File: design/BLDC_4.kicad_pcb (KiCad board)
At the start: 2 copper layers, 233 parts, among them K1 SERVO, P1 CANBUS, P10 MOTOR3, P11 MOTOR2, P12 MOTOR1, P13 SWD, P14 IN+, P15 PWR_COMM, P2 HALL/Encoder, P3 HALL/Encoder, P4 PWR_COMM, P5 IN+, P6 IN-, P7 MOTOR3, P8 MOTOR2, P9 MOTOR1, Q1 IRFS3006, Q10 IRFS3006, Q11 IRFS3006, Q12 IRFS3006, Q2 IRFS3006, Q3 IRFS3006, Q4 IRFS3006, Q5 IRFS3006, Q6 IRFS3006, Q7 IRFS3006, Q8 IRFS3006, Q9 IRFS3006, U1 SN65HVD232, U2 DRV8302, U3 NCP1117ST33T3G, U4 STM32F40X_LQFP144, U5 DRV8302, U6 NCP1117ST33T3G, X1 MINI-USB-SHIELD-32005-201, X2 8MHz 10ppm

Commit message: Start work on pcb
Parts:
- C40, C46, L1, L2, P13, P3, P6, R11, R12, U1, U3, U6, X2: moved to B.Cu
- P15: value PWR_COMM -> PWR_COMM_2; moved to B.Cu
- P4: value PWR_COMM -> PWR_COMM_1
- Q1, Q11, Q3, Q5, Q7, Q9: value IRFS3006 -> FDBL0630N150; footprint CRF1:D2PAK-7-GDS -> H-PSOF:H-PSOF-8L
- Q10, Q12, Q2, Q4, Q6, Q8: value IRFS3006 -> FDBL0630N150; footprint CRF1:D2PAK-7-GDS -> H-PSOF:H-PSOF-8L; moved to B.Cu
- U4: footprint Housings_QFP:TQFP-144_20x20mm_Pitch0.5mm -> Housings_QFP:LQFP-144_20x20mm_Pitch0.5mm
- moved R108 192.1 mm to (142.0, 189.7)
- moved R25 191.9 mm to (117.4, 189.3)
- moved R109 187.5 mm to (146.1, 189.7)
- moved R26 186.7 mm to (121.5, 189.3)
- moved C4 183.0 mm to (116.3, 191.9)
- moved R97 160.8 mm to (170.0, 189.6)
- moved R96 160.7 mm to (165.9, 189.6)
- moved C75 158.2 mm to (108.2, 179.9)
- moved P13 155.6 mm to (67.8, 66.3), turned to 180 degrees
- moved R69 155.3 mm to (118.3, 181.1)
- moved R73 153.6 mm to (123.4, 178.4)
- moved C55 152.1 mm to (122.3, 181.8)
- moved R49 151.5 mm to (169.6, 181.6)
- moved R48 148.2 mm to (173.7, 181.6)
- moved C40 147.0 mm to (80.8, 78.3)
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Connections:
- P15 pad 1: /MCU/RX_SCL_1 -> /MCU/RX_SCL_2
- P15 pad 2: /MCU/TX_SDA_1 -> /MCU/TX_SDA_2
- P15 pad 3: /MCU/ADC_EXT_1 -> /MCU/ADC_EXT_2
- U4 pad 119: /MCU/TX_SDA_1 -> /MCU/TX_SDA_2
- U4 pad 122: /MCU/RX_SCL_1 -> /MCU/RX_SCL_2
- U4 pad 47: /MCU/ADC_EXT_1 -> /MCU/ADC_EXT_2
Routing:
- net /Mosfet driver_2/BR_SO2: track 0.00 -> 52.5 mm, vias 0 -> 2
- net /Mosfet driver_2/BR_SO1: track 0.00 -> 51.2 mm
- net /Mosfet driver_2/L3: track 0.00 -> 47.9 mm, vias 0 -> 2
- net /MCU/ADC_EXT_2: track 0.00 -> 45.5 mm, vias 0 -> 2
- net /Mosfet driver_2/DC_CAL: track 0.00 -> 43.2 mm, vias 0 -> 3
- net /MCU/ADC_EXT_1: track 0.00 -> 37.9 mm, vias 0 -> 2
- net /Mosfet driver_2/EN_GATE: track 0.00 -> 34.9 mm, vias 0 -> 2
- net /Mosfet driver/BR_SO1: track 0.00 -> 25.6 mm
- net /Mosfet driver_2/H3: track 0.00 -> 24.0 mm, vias 0 -> 2
- net /Mosfet driver_2/H1: track 0.00 -> 22.2 mm, vias 0 -> 2
- net /Mosfet driver_2/H2: track 0.00 -> 21.9 mm, vias 0 -> 2
- net /Mosfet driver_2/L2: track 0.00 -> 21.4 mm, vias 0 -> 2
- net /Mosfet driver/BR_SO2: track 0.00 -> 20.2 mm
- net /Mosfet driver_2/L1: track 0.00 -> 19.6 mm
- net Net-(C40-Pad1): track 0.00 -> 16.3 mm, vias 0 -> 1
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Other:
- board outline added: 103 x 63 mm
- copper layers 2 -> 4
- net class Default: clearance 0.254 -> 0.11
- rule trace_clearance: 0.254 -> 0.11

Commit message: PCB
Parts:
- C1, C11, C12, C14, C15, C19, C2, C20, C21, C22, C23, C26, C27, C28, C3, C37, C38, C39, C41, C43, C44, C45, C5, C9, D4, D6, P5, R1, R13, R15, R16, R18, R19, R2, R21, R22, R23, R24, R26, R3, R31, R32, R33, R37, R39, R4, R41, R42, R43, R5, R56, R57, R58, R60, R61, R63, R64, R66, R67, R7, R9, R93, R94, R95, R96, R97: moved to B.Cu
- P13, P15, P3, U3, U6: moved to F.Cu
- moved R27 165.1 mm to (47.9, 68.3), turned to 270 degrees
- moved R33 164.1 mm to (49.9, 68.3), turned to 270 degrees
- moved C5 162.5 mm to (59.0, 64.7), turned to 180 degrees
- moved C7 162.1 mm to (54.0, 73.2), turned to 270 degrees
- moved R95 161.5 mm to (58.4, 93.9), turned to 90 degrees
- moved C8 161.1 mm to (52.4, 73.2), turned to 270 degrees
- moved R30 160.4 mm to (49.9, 68.3), turned to 270 degrees
- moved R32 160.0 mm to (51.9, 68.3), turned to 270 degrees
- moved C36 159.9 mm to (40.1, 78.9), turned to 90 degrees
- moved C6 159.5 mm to (55.7, 73.1), turned to 270 degrees
- moved R57 158.1 mm to (41.9, 69.2)
- moved R56 157.4 mm to (41.9, 67.2)
- moved R58 157.1 mm to (41.9, 71.2)
- moved C39 156.8 mm to (45.4, 72.6), turned to 270 degrees
- moved R29 156.3 mm to (51.9, 68.3), turned to 270 degrees
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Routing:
- net +5V: track 0.00 -> 126.2 mm, vias 0 -> 4
- net GND: track 0.00 -> 85.6 mm, vias 0 -> 8
- net /Mosfet driver_2/BR_SO2: track 52.5 -> 0.00 mm, vias 2 -> 0
- net /Mosfet driver_2/BR_SO1: track 51.2 -> 0.00 mm
- net /Mosfet driver_2/L3: track 47.9 -> 0.00 mm, vias 2 -> 0
- net /Mosfet driver/DC_CAL: track 0.00 -> 46.4 mm, vias 0 -> 2
- net /MCU/ADC_EXT_2: track 45.5 -> 0.00 mm, vias 2 -> 0
- net Net-(C20-Pad1): track 0.00 -> 45.4 mm, vias 0 -> 1
- net /Mosfet driver_2/DC_CAL: track 43.2 -> 0.00 mm, vias 3 -> 0
- net /Mosfet driver/Voltage_divider.sch/OUT: track 0.00 -> 41.7 mm, vias 0 -> 5
- net /Mosfet driver/H3_LOW: track 0.00 -> 38.1 mm, vias 0 -> 5
- net /MCU/ADC_EXT_1: track 37.9 -> 0.00 mm, vias 2 -> 0
- net /Mosfet driver/M_L3: track 0.00 -> 37.2 mm, vias 0 -> 1
- net /MCU/TX_SDA_2: track 0.00 -> 35.1 mm, vias 0 -> 1
- net /Mosfet driver_2/EN_GATE: track 34.9 -> 0.00 mm, vias 2 -> 0
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
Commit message: Layout all on pcb except some resitors
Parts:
- C30, C31, C32, C33, C34, C35, C36, C47, C48, C49, C50, C51, C53, C54, C56, C62, C63, C64, C65, C66, C67, C69, C70, C76, C78, D5, D7, R6, R68, R69, R70, R77, R87, R88, R89: moved to B.Cu
- R93: moved to F.Cu
- moved R88 153.0 mm to (61.6, 92.9), turned to 90 degrees
- moved R87 151.6 mm to (70.0, 92.4), turned to 90 degrees
- moved R89 150.9 mm to (61.9, 90.4), turned to 270 degrees
- moved R86 150.1 mm to (67.7, 92.5), turned to 90 degrees
- moved R92 141.5 mm to (74.8, 92.7), turned to 90 degrees
- moved C74 109.8 mm to (117.8, 71.2), turned to 90 degrees
- moved C75 109.3 mm to (115.2, 70.8), turned to 90 degrees
- moved C58 107.9 mm to (108.5, 75.5)
- moved R69 107.8 mm to (110.6, 73.6)
- moved C76 106.5 mm to (122.1, 70.2), turned to 270 degrees
- moved C55 105.9 mm to (112.6, 76.4), turned to 180 degrees
- moved C69 105.7 mm to (130.1, 71.8), turned to 270 degrees
- moved C70 105.6 mm to (127.7, 72.2), turned to 90 degrees
- moved R73 101.8 mm to (123.2, 76.6), turned to 180 degrees
- moved C53 101.6 mm to (124.4, 74.9)
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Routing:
- net (no net): track 1.11 -> 144.9 mm, vias 0 -> 3
- net +5V: track 126.2 -> 32.5 mm, vias 4 -> 2
- net V_SUPPLY: track 19.6 -> 67.2 mm, vias 1 -> 2
- net /Mosfet driver/DC_CAL: track 46.4 -> 0.00 mm, vias 2 -> 0
- net /Mosfet driver/Voltage_divider.sch/OUT: track 41.7 -> 0.00 mm, vias 5 -> 0
- net /Mosfet driver/H3_LOW: track 38.1 -> 0.00 mm, vias 5 -> 0
- net /Mosfet driver/M_L3: track 37.2 -> 0.00 mm, vias 1 -> 0
- net GND: track 85.6 -> 121.7 mm, vias 8 -> 9
- net /MCU/TX_SDA_2: track 35.1 -> 0.00 mm, vias 1 -> 0
- net /MCU/RX_SCL_2: track 34.6 -> 0.00 mm, vias 2 -> 0
- net Net-(Q1-PadG): track 34.4 -> 0.00 mm
- net SWCLK: track 32.7 -> 0.00 mm, vias 2 -> 0
- net Net-(Q7-PadG): track 30.6 -> 0.00 mm
- net /Mosfet driver_2/M_H1: track 30.5 -> 0.00 mm
- net /Mosfet driver_2/M_L1: track 30.3 -> 0.00 mm, vias 1 -> 0
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
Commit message: Add all components
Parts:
- C61, R101, R109, R50, R80: moved to B.Cu
- moved R50 127.5 mm to (77.0, 92.2), turned to 90 degrees
- moved R51 123.4 mm to (76.6, 94.0), turned to 90 degrees
- moved R81 93.3 mm to (86.8, 95.6), turned to 90 degrees
- moved R80 89.9 mm to (87.5, 95.0), turned to 180 degrees
- moved R100 89.6 mm to (114.5, 92.5), turned to 90 degrees
- moved R98 88.8 mm to (112.3, 92.7), turned to 90 degrees
- moved R101 88.3 mm to (115.5, 92.0), turned to 180 degrees
- moved R85 87.8 mm to (83.2, 97.7), turned to 180 degrees
- moved R84 86.9 mm to (80.9, 97.3), turned to 90 degrees
- moved R102 85.2 mm to (106.0, 95.8), turned to 270 degrees
- moved R99 83.8 mm to (112.5, 95.4), turned to 90 degrees
- moved R103 82.1 mm to (107.6, 96.0), turned to 90 degrees
- moved R83 81.3 mm to (103.5, 96.2), turned to 90 degrees
- moved R82 80.8 mm to (101.3, 96.2), turned to 90 degrees
- moved R109 80.3 mm to (119.9, 96.6), turned to 180 degrees
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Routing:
- net VCC: track 21.0 -> 303.2 mm, vias 2 -> 26
- net +5V: track 32.5 -> 193.3 mm, vias 2 -> 11
- net V_SUPPLY: track 67.2 -> 83.6 mm, vias 2 -> 3
- net GND: track 121.7 -> 110.3 mm
- net Net-(C42-Pad1): track 5.38 -> 1.03 mm
- net /Mosfet driver_2/SENS3: track 0.00 -> 2.00 mm
- net Net-(D3-Pad1): track 1.75 -> 3.36 mm
- net /Mosfet driver_2/SH2_A: track 0.82 -> 0.00 mm
- net Net-(C68-Pad1): track 5.12 -> 5.94 mm
- net (no net): track 144.9 -> 145.4 mm

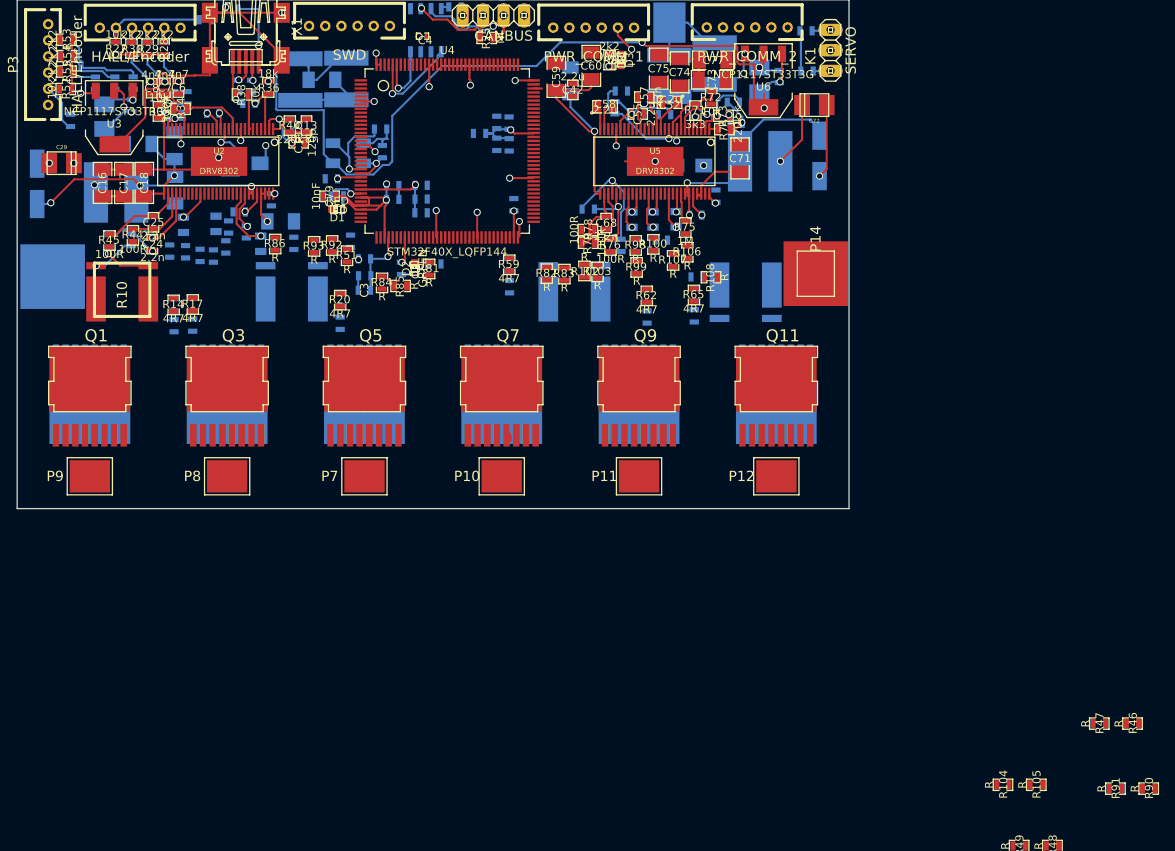
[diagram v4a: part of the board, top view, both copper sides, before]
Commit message: Routing ... Maybe H_VS and other dividers are to close to chip and one another it's a 100V.
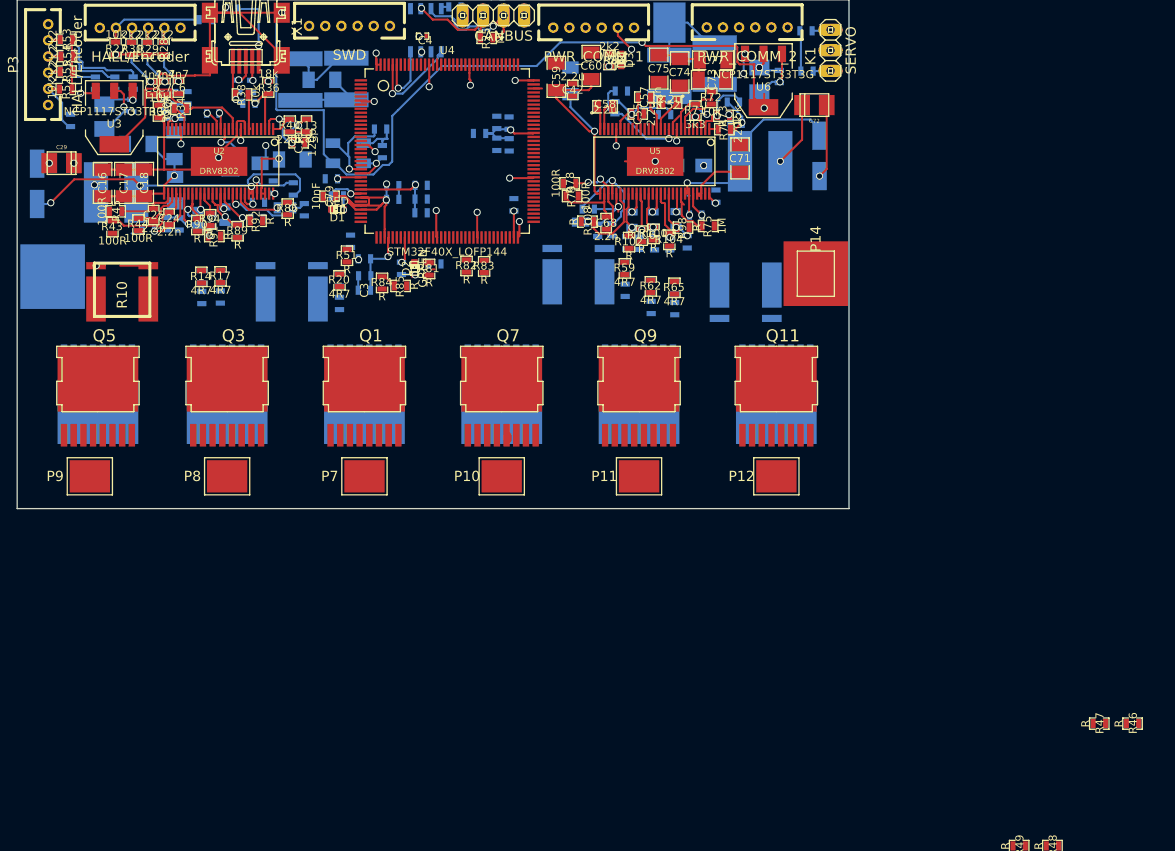
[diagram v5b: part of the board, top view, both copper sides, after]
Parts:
- R103, R105, R107, R76, R93, R99: moved to B.Cu
- R43, R89, R94: moved to F.Cu
- moved R90 136.9 mm to (58.0, 90.2), turned to 90 degrees
- moved R91 130.9 mm to (60.2, 91.5), turned to 180 degrees
- moved R105 80.9 mm to (116.6, 92.5), turned to 90 degrees
- moved R104 79.1 mm to (116.5, 92.0), turned to 90 degrees
- moved Q1 34.0 mm to (78.8, 113.3)
- moved Q2 34.0 mm to (78.8, 109.3)
- moved Q5 33.0 mm to (45.8, 113.3)
- moved Q6 33.0 mm to (45.8, 109.3)
- moved R108 16.8 mm to (106.4, 89.7), turned to 0 degrees
- moved R109 15.9 mm to (105.5, 89.8), turned to 0 degrees
- moved R60 14.3 mm to (111.0, 95.5)
- moved R61 14.3 mm to (111.0, 98.2)
- moved R59 14.3 mm to (111.0, 95.5)
- moved R83 9.99 mm to (93.6, 95.3)
- moved R82 9.99 mm to (91.4, 95.2)
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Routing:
- net /Mosfet driver/Voltage_divider.sch/OUT: track 0.00 -> 47.3 mm, vias 0 -> 8
- net /Mosfet driver_2/Voltage_divider.sch/OUT: track 13.8 -> 41.1 mm, vias 3 -> 7
- net Net-(C20-Pad1): track 29.6 -> 40.1 mm
- net GND: track 110.3 -> 118.0 mm
- net Net-(C68-Pad1): track 5.94 -> 10.8 mm, vias 0 -> 2
- net /Mosfet driver/SH1_A: track 5.41 -> 1.10 mm
- net Net-(C24-Pad1): track 3.53 -> 7.76 mm
- net Net-(C20-Pad2): track 2.98 -> 6.75 mm
- net Net-(C22-Pad2): track 0.00 -> 3.71 mm, vias 0 -> 1
- net V_SUPPLY: track 83.6 -> 86.8 mm
- net /Mosfet driver/SH1_B: track 6.47 -> 3.47 mm, vias 1 -> 0
- net Net-(R75-Pad2): track 3.65 -> 6.31 mm
- net Net-(R41-Pad2): track 4.73 -> 2.12 mm
- net Net-(C25-Pad2): track 10.1 -> 7.59 mm
- net VCC: track 303.2 -> 305.2 mm, vias 26 -> 27
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
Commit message: New pcb layout
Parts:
- C1, C11, C12, C14, C15, C19, C2, C20, C21, C22, C23, C26, C27, C28, C3, C30, C31, C32, C34, C36, C37, C38, C39, C40, C41, C43, C44, C45, C46, C47, C48, C49, C5, C50, C51, C53, C54, C56, C61, C62, C63, C64, C65, C66, C67, C69, C70, C76, C9, D4, D5, D6, D7, L1, L2, P5, P6, R1, R101, R103, R105, R107, R109, R13, R15, R16, R18, R19, R2, R21, R22, R23, R24, R26, R3, R31, R32, R33, R37, R39, R4, R41, R42, R5, R50, R56, R57, R58, R6, R60, R61, R63, R64, R66, R67, R68, R69, R7, R70, R76, R77, R80, R87, R88, R9, R93, R95, R96, R97, R99, X2: moved to F.Cu
- P10, P11, P12, P7, P8, P9: moved to B.Cu
- moved R53 228.2 mm to (184.4, 245.5)
- moved R97 227.1 mm to (200.3, 264.0), turned to 0 degrees
- moved R94 226.9 mm to (213.9, 255.9), turned to 0 degrees
- moved R54 226.6 mm to (180.3, 248.7)
- moved R91 226.4 mm to (233.3, 237.5), turned to 0 degrees
- moved R52 226.1 mm to (180.3, 252.0)
- moved R88 226.0 mm to (225.8, 247.9), turned to 0 degrees
- moved R90 225.8 mm to (229.2, 237.5), turned to 0 degrees
- moved R56 225.7 mm to (180.3, 245.5)
- moved R55 225.3 mm to (176.2, 252.0)
- moved C36 225.2 mm to (184.4, 251.9), turned to 0 degrees
- moved C39 224.3 mm to (184.4, 248.7), turned to 0 degrees
- moved R57 224.2 mm to (176.2, 248.7)
- moved R92 224.0 mm to (240.5, 229.4), turned to 0 degrees
- moved R95 223.9 mm to (209.8, 255.9), turned to 0 degrees
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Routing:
- net VCC: track 305.2 -> 0.00 mm, vias 27 -> 0
- net +5V: track 193.3 -> 0.00 mm, vias 11 -> 0
- net (no net): track 145.4 -> 0.00 mm, vias 3 -> 0
- net GND: track 118.0 -> 0.00 mm, vias 9 -> 0
- net V_SUPPLY: track 86.8 -> 0.00 mm, vias 3 -> 0
- net /Mosfet driver/Voltage_divider.sch/OUT: track 47.3 -> 0.00 mm, vias 8 -> 0
- net /Mosfet driver_2/Voltage_divider.sch/OUT: track 41.1 -> 0.00 mm, vias 7 -> 0
- net Net-(C20-Pad1): track 40.1 -> 0.00 mm, vias 3 -> 0
- net Net-(C63-Pad1): track 28.2 -> 0.00 mm, vias 2 -> 0
- net Net-(R34-Pad2): track 14.8 -> 0.00 mm
- net Net-(C67-Pad2): track 13.7 -> 0.00 mm, vias 1 -> 0
- net Net-(R68-Pad2): track 13.2 -> 0.00 mm, vias 1 -> 0
- net /Filters/TEMP_IN: track 12.5 -> 0.00 mm
- net Net-(C40-Pad1): track 11.7 -> 0.00 mm, vias 1 -> 0
- net Net-(C24-Pad2): track 11.3 -> 0.00 mm
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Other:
- board size 103 x 63 mm -> 141 x 61 mm
